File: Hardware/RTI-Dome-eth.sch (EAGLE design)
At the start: 85 parts, among them IC1 24AA128ST, IC3 FT232RL, IC4 REG1117, IC5 74LVC245, IC6 74ABT245, J1 POWERPOLE_POWER45A, U1 W5500, X13 PN61729-S, X9 J1011F21PNL

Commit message: Re-did some of the core to receive data from network and wireless connection
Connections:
- net GND: now also R14.1
- net VCC: no longer R14.1
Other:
- moved on the sheet: R14
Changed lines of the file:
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@@
 <part name="FRAME2" library="frames" deviceset="DINA3_L" device=""/>
 <part name="GND16" library="supply1" deviceset="GND" device=""/>
+<part name="GND21" library="supply1" deviceset="GND" device=""/>
 </parts>
 <sheets>
@@
 <attribute name="MPN" x="312.42" y="241.3" size="1.778" layer="96" rot="R90" display="off"/>
 </instance>
-<instance part="R14" gate="G$1" x="297.18" y="241.3" rot="R270">
-<attribute name="MPN" x="297.18" y="241.3" size="1.778" layer="96" rot="R270" display="off"/>
+<instance part="R14" gate="G$1" x="236.22" y="210.82" rot="R270">
+<attribute name="MPN" x="236.22" y="210.82" size="1.778" layer="96" rot="R270" display="off"/>
 </instance>
 <instance part="R15" gate="G$1" x="281.94" y="241.3" rot="R270">
@@
 <instance part="GND18" gate="1" x="38.1" y="55.88"/>
 <instance part="GND16" gate="1" x="116.84" y="223.52"/>
+<instance part="GND21" gate="1" x="226.06" y="210.82"/>
 </instances>
 <busses>
@@
 <pinref part="GND16" gate="1" pin="GND"/>
 </segment>
+<segment>
+<pinref part="R14" gate="G$1" pin="1"/>
+<wire x1="236.22" y1="215.9" x2="236.22" y2="218.44" width="0.1524" layer="91"/>
+<wire x1="236.22" y1="218.44" x2="226.06" y2="218.44" width="0.1524" layer="91"/>
+<wire x1="226.06" y1="218.44" x2="226.06" y2="213.36" width="0.1524" layer="91"/>
+<pinref part="GND21" gate="1" pin="GND"/>
+</segment>
 </net>
 <net name="+12V" class="1">
@@
 <net name="M_EN_5V" class="0">
 <segment>
-<label x="297.18" y="233.68" size="1.016" layer="95" rot="R270" xref="yes"/>
-<wire x1="297.18" y1="233.68" x2="297.18" y2="236.22" width="0.1524" layer="91"/>
+<label x="236.22" y="203.2" size="1.016" layer="95" rot="R270" xref="yes"/>
+<wire x1="236.22" y1="203.2" x2="236.22" y2="205.74" width="0.1524" layer="91"/>
 <pinref part="R14" gate="G$1" pin="2"/>
 </segment>
@@
 <wire x1="289.56" y1="246.38" x2="289.56" y2="248.92" width="0.1524" layer="91"/>
 <junction x="289.56" y="248.92"/>
-<pinref part="R14" gate="G$1" pin="1"/>
-<wire x1="297.18" y1="246.38" x2="297.18" y2="248.92" width="0.1524" layer="91"/>
-<junction x="297.18" y="248.92"/>
 <pinref part="R19" gate="G$1" pin="1"/>
 <wire x1="304.8" y1="246.38" x2="304.8" y2="248.92" width="0.1524" layer="91"/>

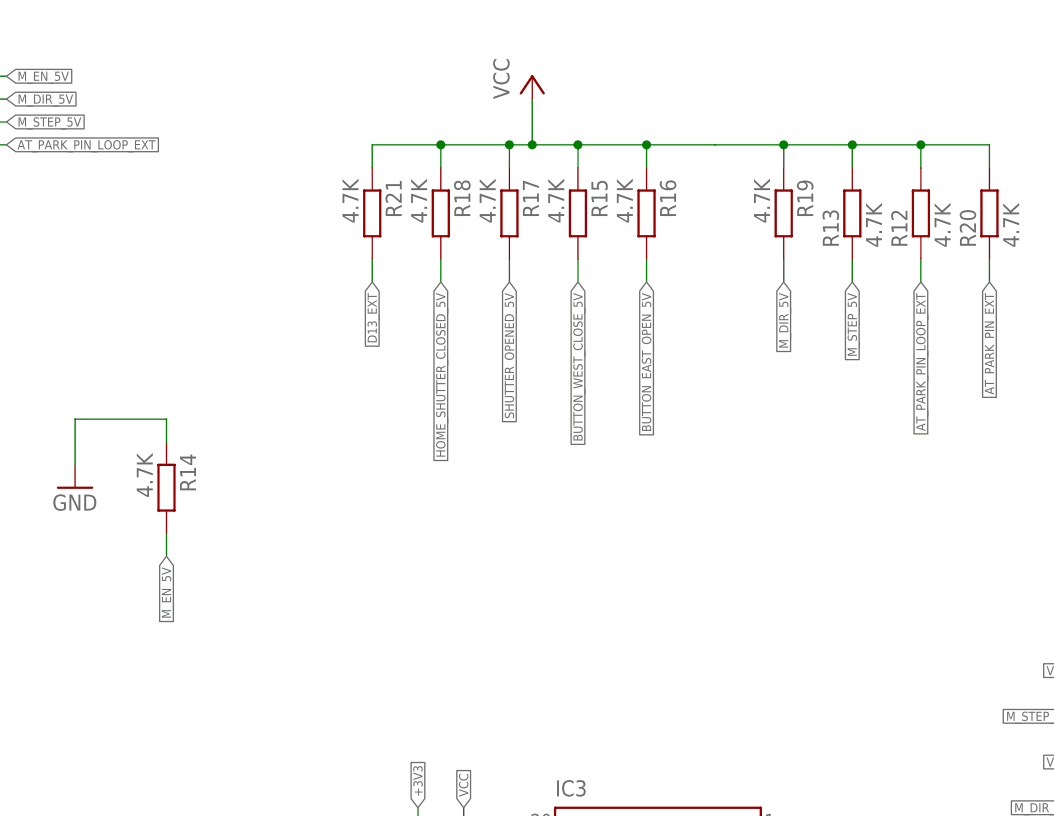
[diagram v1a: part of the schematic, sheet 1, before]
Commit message: Making some pull-up pull-down to get a better OFF state when the controller is not powered but the stepper driver is.
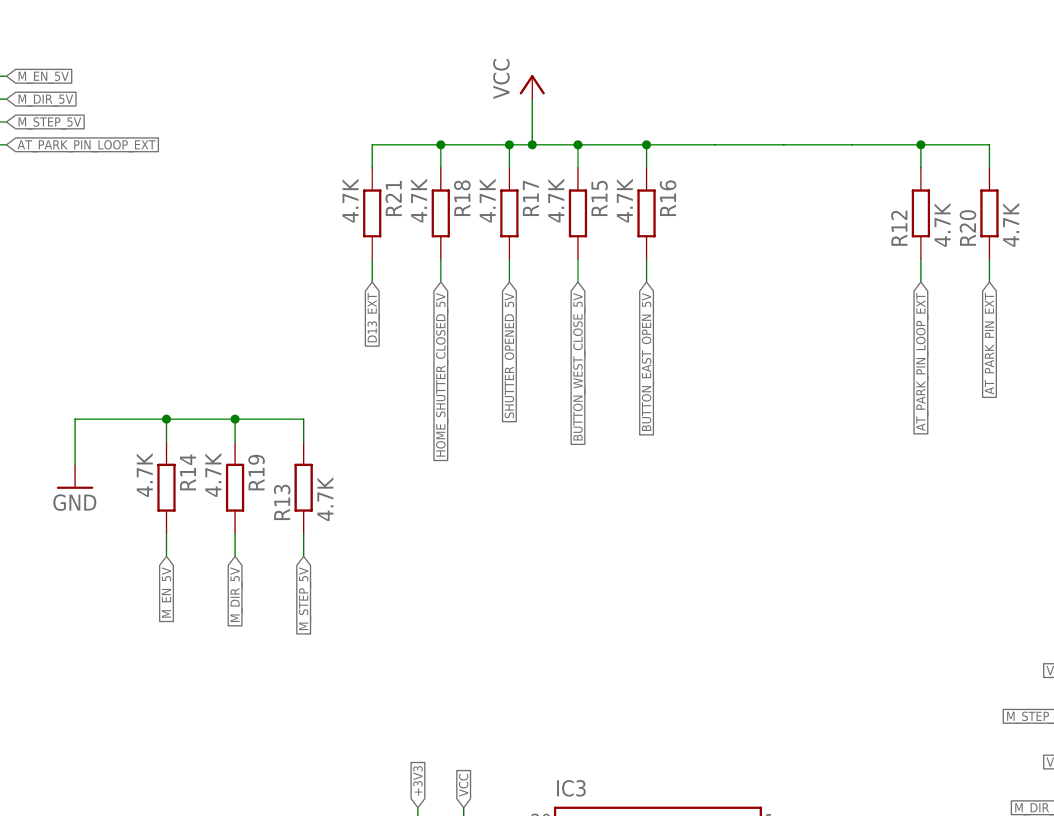
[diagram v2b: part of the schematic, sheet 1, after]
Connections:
- net GND: now also R13.2, R19.1
- net VCC: no longer R13.2, R19.1
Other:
- moved on the sheet: R13, R19
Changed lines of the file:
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@@
 <instance part="GND4" gate="1" x="368.3" y="45.72"/>
 <instance part="P+4" gate="VCC" x="276.86" y="256.54"/>
-<instance part="R13" gate="G$1" x="312.42" y="241.3" rot="R90">
-<attribute name="MPN" x="312.42" y="241.3" size="1.778" layer="96" rot="R90" display="off"/>
+<instance part="R13" gate="G$1" x="251.46" y="210.82" rot="R90">
+<attribute name="MPN" x="251.46" y="210.82" size="1.778" layer="96" rot="R90" display="off"/>
 </instance>
 <instance part="R14" gate="G$1" x="236.22" y="210.82" rot="R270">
@@
 <attribute name="MPN" x="266.7" y="241.3" size="1.778" layer="96" rot="R270" display="off"/>
 </instance>
-<instance part="R19" gate="G$1" x="304.8" y="241.3" rot="R270">
-<attribute name="MPN" x="304.8" y="241.3" size="1.778" layer="96" rot="R270" display="off"/>
+<instance part="R19" gate="G$1" x="243.84" y="210.82" rot="R270">
+<attribute name="MPN" x="243.84" y="210.82" size="1.778" layer="96" rot="R270" display="off"/>
 </instance>
 <instance part="R6" gate="G$1" x="7.62" y="195.58" rot="R90">
@@
 <wire x1="226.06" y1="218.44" x2="226.06" y2="213.36" width="0.1524" layer="91"/>
 <pinref part="GND21" gate="1" pin="GND"/>
+<pinref part="R13" gate="G$1" pin="2"/>
+<wire x1="236.22" y1="218.44" x2="243.84" y2="218.44" width="0.1524" layer="91"/>
+<wire x1="243.84" y1="218.44" x2="251.46" y2="218.44" width="0.1524" layer="91"/>
+<wire x1="251.46" y1="218.44" x2="251.46" y2="215.9" width="0.1524" layer="91"/>
+<junction x="236.22" y="218.44"/>
+<pinref part="R19" gate="G$1" pin="1"/>
+<wire x1="243.84" y1="218.44" x2="243.84" y2="215.9" width="0.1524" layer="91"/>
+<junction x="243.84" y="218.44"/>
 </segment>
 </net>
@@
 <net name="M_STEP_5V" class="0">
 <segment>
-<wire x1="312.42" y1="233.68" x2="312.42" y2="236.22" width="0.1524" layer="91"/>
-<label x="312.42" y="233.68" size="1.016" layer="95" rot="R270" xref="yes"/>
+<wire x1="251.46" y1="203.2" x2="251.46" y2="205.74" width="0.1524" layer="91"/>
+<label x="251.46" y="203.2" size="1.016" layer="95" rot="R270" xref="yes"/>
 <pinref part="R13" gate="G$1" pin="1"/>
 </segment>
@@
 <net name="M_DIR_5V" class="0">
 <segment>
-<label x="304.8" y="233.68" size="1.016" layer="95" rot="R270" xref="yes"/>
-<wire x1="304.8" y1="233.68" x2="304.8" y2="236.22" width="0.1524" layer="91"/>
+<label x="243.84" y="203.2" size="1.016" layer="95" rot="R270" xref="yes"/>
+<wire x1="243.84" y1="203.2" x2="243.84" y2="205.74" width="0.1524" layer="91"/>
 <pinref part="R19" gate="G$1" pin="2"/>
 </segment>
@@
 <wire x1="266.7" y1="246.38" x2="266.7" y2="248.92" width="0.1524" layer="91"/>
 <wire x1="266.7" y1="248.92" x2="274.32" y2="248.92" width="0.1524" layer="91"/>
-<pinref part="R13" gate="G$1" pin="2"/>
 <wire x1="274.32" y1="248.92" x2="276.86" y2="248.92" width="0.1524" layer="91"/>
 <wire x1="276.86" y1="248.92" x2="281.94" y2="248.92" width="0.1524" layer="91"/>
@@
 <wire x1="297.18" y1="248.92" x2="304.8" y2="248.92" width="0.1524" layer="91"/>
 <wire x1="304.8" y1="248.92" x2="312.42" y2="248.92" width="0.1524" layer="91"/>
-<wire x1="312.42" y1="248.92" x2="312.42" y2="246.38" width="0.1524" layer="91"/>
 <junction x="276.86" y="248.92"/>
 <pinref part="R17" gate="G$1" pin="1"/>
@@
 <wire x1="289.56" y1="246.38" x2="289.56" y2="248.92" width="0.1524" layer="91"/>
 <junction x="289.56" y="248.92"/>
-<pinref part="R19" gate="G$1" pin="1"/>
-<wire x1="304.8" y1="246.38" x2="304.8" y2="248.92" width="0.1524" layer="91"/>
-<junction x="304.8" y="248.92"/>
 <pinref part="R20" gate="G$1" pin="2"/>
 <wire x1="312.42" y1="248.92" x2="320.04" y2="248.92" width="0.1524" layer="91"/>
 <wire x1="320.04" y1="248.92" x2="327.66" y2="248.92" width="0.1524" layer="91"/>
 <wire x1="327.66" y1="248.92" x2="327.66" y2="246.38" width="0.1524" layer="91"/>
-<junction x="312.42" y="248.92"/>
 <pinref part="R12" gate="G$1" pin="2"/>
 <wire x1="320.04" y1="248.92" x2="320.04" y2="246.38" width="0.1524" layer="91"/>

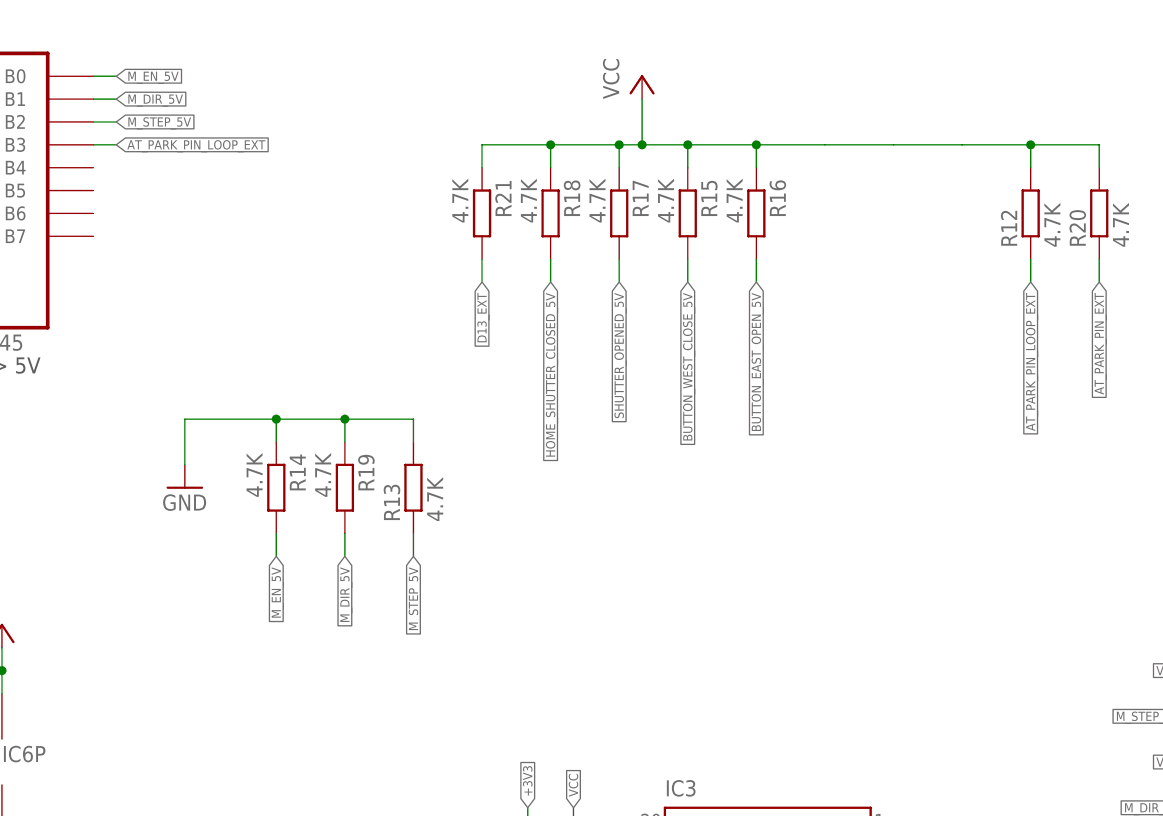
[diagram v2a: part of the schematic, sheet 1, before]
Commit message: Pull-down doesn't really help. Setting back to pull-up to make sure enable does enable :)
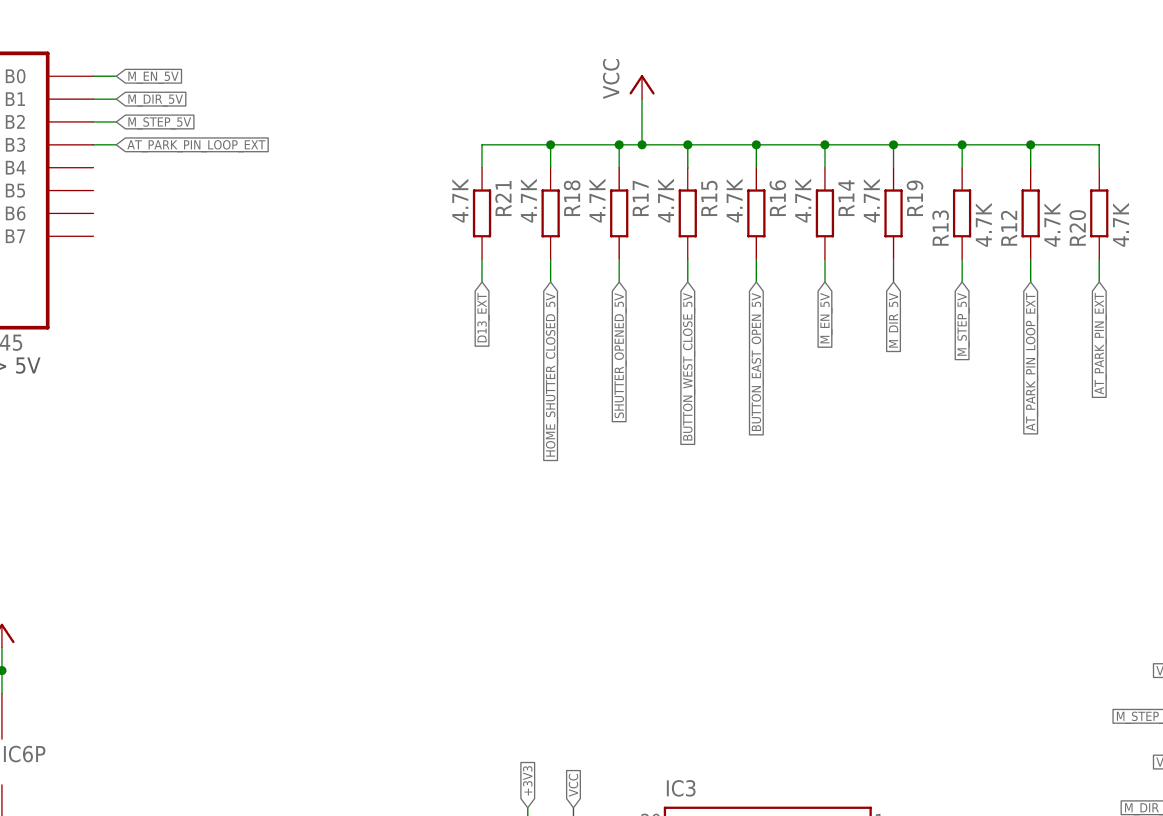
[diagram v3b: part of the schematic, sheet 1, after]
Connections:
- net GND: no longer R13.2, R14.1, R19.1
- net VCC: now also R13.2, R14.1, R19.1
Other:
- moved on the sheet: R13, R14, R19
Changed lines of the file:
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@@
 <part name="FRAME2" library="frames" deviceset="DINA3_L" device=""/>
 <part name="GND16" library="supply1" deviceset="GND" device=""/>
-<part name="GND21" library="supply1" deviceset="GND" device=""/>
 </parts>
 <sheets>
@@
 <instance part="GND4" gate="1" x="368.3" y="45.72"/>
 <instance part="P+4" gate="VCC" x="276.86" y="256.54"/>
-<instance part="R13" gate="G$1" x="251.46" y="210.82" rot="R90">
-<attribute name="MPN" x="251.46" y="210.82" size="1.778" layer="96" rot="R90" display="off"/>
-</instance>
-<instance part="R14" gate="G$1" x="236.22" y="210.82" rot="R270">
-<attribute name="MPN" x="236.22" y="210.82" size="1.778" layer="96" rot="R270" display="off"/>
+<instance part="R13" gate="G$1" x="312.42" y="241.3" rot="R90">
+<attribute name="MPN" x="312.42" y="241.3" size="1.778" layer="96" rot="R90" display="off"/>
+</instance>
+<instance part="R14" gate="G$1" x="297.18" y="241.3" rot="R270">
+<attribute name="MPN" x="297.18" y="241.3" size="1.778" layer="96" rot="R270" display="off"/>
 </instance>
 <instance part="R15" gate="G$1" x="281.94" y="241.3" rot="R270">
@@
 <attribute name="MPN" x="266.7" y="241.3" size="1.778" layer="96" rot="R270" display="off"/>
 </instance>
-<instance part="R19" gate="G$1" x="243.84" y="210.82" rot="R270">
-<attribute name="MPN" x="243.84" y="210.82" size="1.778" layer="96" rot="R270" display="off"/>
+<instance part="R19" gate="G$1" x="304.8" y="241.3" rot="R270">
+<attribute name="MPN" x="304.8" y="241.3" size="1.778" layer="96" rot="R270" display="off"/>
 </instance>
 <instance part="R6" gate="G$1" x="7.62" y="195.58" rot="R90">
@@
 <instance part="GND18" gate="1" x="38.1" y="55.88"/>
 <instance part="GND16" gate="1" x="116.84" y="223.52"/>
-<instance part="GND21" gate="1" x="226.06" y="210.82"/>
 </instances>
 <busses>
@@
 <pinref part="GND16" gate="1" pin="GND"/>
 </segment>
-<segment>
-<pinref part="R14" gate="G$1" pin="1"/>
-<wire x1="236.22" y1="215.9" x2="236.22" y2="218.44" width="0.1524" layer="91"/>
-<wire x1="236.22" y1="218.44" x2="226.06" y2="218.44" width="0.1524" layer="91"/>
-<wire x1="226.06" y1="218.44" x2="226.06" y2="213.36" width="0.1524" layer="91"/>
-<pinref part="GND21" gate="1" pin="GND"/>
-<pinref part="R13" gate="G$1" pin="2"/>
-<wire x1="236.22" y1="218.44" x2="243.84" y2="218.44" width="0.1524" layer="91"/>
-<wire x1="243.84" y1="218.44" x2="251.46" y2="218.44" width="0.1524" layer="91"/>
-<wire x1="251.46" y1="218.44" x2="251.46" y2="215.9" width="0.1524" layer="91"/>
-<junction x="236.22" y="218.44"/>
-<pinref part="R19" gate="G$1" pin="1"/>
-<wire x1="243.84" y1="218.44" x2="243.84" y2="215.9" width="0.1524" layer="91"/>
-<junction x="243.84" y="218.44"/>
-</segment>
 </net>
 <net name="+12V" class="1">
@@
 <net name="M_STEP_5V" class="0">
 <segment>
-<wire x1="251.46" y1="203.2" x2="251.46" y2="205.74" width="0.1524" layer="91"/>
-<label x="251.46" y="203.2" size="1.016" layer="95" rot="R270" xref="yes"/>
+<wire x1="312.42" y1="233.68" x2="312.42" y2="236.22" width="0.1524" layer="91"/>
+<label x="312.42" y="233.68" size="1.016" layer="95" rot="R270" xref="yes"/>
 <pinref part="R13" gate="G$1" pin="1"/>
 </segment>
@@
 <net name="M_DIR_5V" class="0">
 <segment>
-<label x="243.84" y="203.2" size="1.016" layer="95" rot="R270" xref="yes"/>
-<wire x1="243.84" y1="203.2" x2="243.84" y2="205.74" width="0.1524" layer="91"/>
+<label x="304.8" y="233.68" size="1.016" layer="95" rot="R270" xref="yes"/>
+<wire x1="304.8" y1="233.68" x2="304.8" y2="236.22" width="0.1524" layer="91"/>
 <pinref part="R19" gate="G$1" pin="2"/>
 </segment>
@@
 <net name="M_EN_5V" class="0">
 <segment>
-<label x="236.22" y="203.2" size="1.016" layer="95" rot="R270" xref="yes"/>
-<wire x1="236.22" y1="203.2" x2="236.22" y2="205.74" width="0.1524" layer="91"/>
+<label x="297.18" y="233.68" size="1.016" layer="95" rot="R270" xref="yes"/>
+<wire x1="297.18" y1="233.68" x2="297.18" y2="236.22" width="0.1524" layer="91"/>
 <pinref part="R14" gate="G$1" pin="2"/>
 </segment>
@@
 <wire x1="259.08" y1="248.92" x2="259.08" y2="246.38" width="0.1524" layer="91"/>
 <junction x="266.7" y="248.92"/>
-</segment>
-<segment>
+<pinref part="R14" gate="G$1" pin="1"/>
+<wire x1="297.18" y1="246.38" x2="297.18" y2="248.92" width="0.1524" layer="91"/>
+<junction x="297.18" y="248.92"/>
+<pinref part="R19" gate="G$1" pin="1"/>
+<wire x1="304.8" y1="248.92" x2="304.8" y2="246.38" width="0.1524" layer="91"/>
+<junction x="304.8" y="248.92"/>
+<pinref part="R13" gate="G$1" pin="2"/>
+<wire x1="312.42" y1="248.92" x2="312.42" y2="246.38" width="0.1524" layer="91"/>
+<junction x="312.42" y="248.92"/>
+</segment>
+<segment>
